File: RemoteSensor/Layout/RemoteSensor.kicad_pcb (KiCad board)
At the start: 2 copper layers, 50.8 x 50.8 mm, 47 parts, among them J1 PRG_HEADER, J2 LCD_HEADER, J3 USB_B_Micro, J4 BATT_CONN, Q1 2N7002, Q2 2N7002, Q3 2N7002, SW1 BTN_RST, SW2 BTN_LOAD, SW3 SW_DPDT_x2, U1 ESP-12F, U2 74LVC2G02, U3 LM50CIM3, U4 MCP73831-2-OT, U5 LM3670MF, U6 BD48ExxG, U7 BD48ExxG

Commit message: Edit layout
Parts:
- removed SW3: SW_DPDT_x2, Switches:SWITCH_DPDT_SMD_AYZ0202
- added C10: 100n, Capacitor_SMD:C_0603_1608Metric_Pad1.05x0.95mm_HandSolder, B.Cu at (130.6, 92.3)
- added C7: 4.7u, Capacitor_SMD:C_0603_1608Metric_Pad1.05x0.95mm_HandSolder, F.Cu at (126.5, 73.1)
- added C8: 47p, Capacitor_SMD:C_0603_1608Metric_Pad1.05x0.95mm_HandSolder, F.Cu at (139.5, 74.0)
- added C9: 47p, Capacitor_SMD:C_0603_1608Metric_Pad1.05x0.95mm_HandSolder, F.Cu at (135.9, 74.0)
- added FB1: Ferrite_Bead, Resistor_SMD:R_0603_1608Metric_Pad1.05x0.95mm_HandSolder, B.Cu at (136.9, 97.0)
- added JP1: Jumper_2_Open, Jumper:SolderJumper-2_P1.3mm_Open_Pad1.0x1.5mm, F.Cu at (148.8, 106.5)
- added JP2: Jumper_2_Open, Jumper:SolderJumper-2_P1.3mm_Open_Pad1.0x1.5mm, F.Cu at (154.5, 106.5)
- added Q4: MMBT2222A-TP, digikey-footprints:SOT-23-3, B.Cu at (129.6, 110.5)
- added Q5: MMBT2222A-TP, digikey-footprints:SOT-23-3, B.Cu at (135.8, 110.5)
- added R17: 1k, Resistor_SMD:R_0603_1608Metric_Pad1.05x0.95mm_HandSolder, F.Cu at (124.3, 85.8)
- added R18: 1k, Resistor_SMD:R_0603_1608Metric_Pad1.05x0.95mm_HandSolder, F.Cu at (126.2, 85.8)
- added R19: 10k, Resistor_SMD:R_0603_1608Metric_Pad1.05x0.95mm_HandSolder, B.Cu at (140.0, 87.1)
- added R20: 10k, Resistor_SMD:R_0603_1608Metric_Pad1.05x0.95mm_HandSolder, F.Cu at (135.2, 87.1)
- added R21: 10k, Resistor_SMD:R_0603_1608Metric_Pad1.05x0.95mm_HandSolder, F.Cu at (143.1, 89.9)
- added R22: 10k, Resistor_SMD:R_0603_1608Metric_Pad1.05x0.95mm_HandSolder, F.Cu at (131.3, 87.1)
- added R23: 10k, Resistor_SMD:R_0603_1608Metric_Pad1.05x0.95mm_HandSolder, B.Cu at (135.8, 107.4)
- added R24: 10k, Resistor_SMD:R_0603_1608Metric_Pad1.05x0.95mm_HandSolder, B.Cu at (129.6, 107.4)
- added R25: 27, Resistor_SMD:R_0603_1608Metric_Pad1.05x0.95mm_HandSolder, F.Cu at (141.3, 74.0)
- added R26: 27, Resistor_SMD:R_0603_1608Metric_Pad1.05x0.95mm_HandSolder, F.Cu at (137.7, 74.0)
- added U10: FT231XS, Package_SO:SSOP-20_3.9x8.7mm_P0.635mm, B.Cu at (131.1, 97.0)
- added U8: LM50CIM3, LM50CIM3:SOT95P260X110-3N, F.Cu at (141.4, 111.1)
- added U9: MCP23008-E_P, Package_SO:SOIC-18W_7.5x11.6mm_P1.27mm, B.Cu at (140.3, 80.2)
- C3: value 4.7u -> 10u
- C4: value 10u -> 4.7u
- J1: value PRG_HEADER -> USB_B_Micro; footprint Connector_PinSocket_2.54mm:PinSocket_1x03_P2.54mm_Vertical -> Connector_USB:USB_Micro-B_Molex_47346-0001
- J2: value LCD_HEADER -> BATT_CONN; footprint Connector_PinHeader_2.54mm:PinHeader_1x04_P2.54mm_Vertical -> Connector_JST:JST_PH_S2B-PH-SM4-TB_1x02-1MP_P2.00mm_Horizontal; moved to B.Cu
- J3: value USB_B_Micro -> LCD_HEADER; footprint Connector_USB:USB_Micro-B_Molex_47346-0001 -> Connector_PinHeader_2.54mm:PinHeader_1x04_P2.54mm_Vertical
- J4: value BATT_CONN -> PRG_HEADER; footprint Connector_JST:JST_PH_S2B-PH-SM4-TB_1x02-1MP_P2.00mm_Horizontal -> Connector_PinSocket_2.54mm:PinSocket_1x03_P2.54mm_Vertical; moved to F.Cu
- L1: footprint Inductor_SMD:L_0603_1608Metric_Pad1.05x0.95mm_HandSolder -> Inductor_SMD:L_Taiyo-Yuden_NR-24xx_HandSoldering
- Q3, R15, R2, R3, R4: moved to F.Cu
- R1: value 10k -> 2k; moved to F.Cu
- R10: value 1k -> 10k
- R11: value 1k -> 4.7k
- R12: value 2k -> 100
- R13: value 10k -> 100; moved to F.Cu
- R14: value 10k -> 4.7k; moved to F.Cu
- R5, R6: value 4.7k -> 10k
- R8, R9: value 220 -> 10k
- SW2: value BTN_LOAD -> SW_Push
- U1: value ESP-12F -> MCP73831-2-OT; footprint RF_Module:ESP-12E -> Package_TO_SOT_SMD:SOT-23-5
- U2: value 74LVC2G02 -> LM3671MF; footprint Package_SO:VSSOP-8_2.3x2mm_P0.5mm -> Package_TO_SOT_SMD:TSOT-23-5; moved to F.Cu
- U3: value LM50CIM3 -> BD48ExxG; footprint LM50CIM3:SOT95P260X110-3N -> Package_TO_SOT_SMD:SOT-23-5
- U4: value MCP73831-2-OT -> BD48ExxG
- U5: value LM3670MF -> LM3671MF
- U6: value BD48ExxG -> 74LVC2G02; footprint Package_TO_SOT_SMD:SOT-23-5 -> Package_SO:VSSOP-8_2.3x2mm_P0.5mm; moved to F.Cu
- U7: value BD48ExxG -> ESP-12F; footprint Package_TO_SOT_SMD:SOT-23-5 -> RF_Module:ESP-12E; moved to F.Cu
- moved R16 48.2 mm to (126.4, 107.8), turned to 180 degrees
- moved R12 45.9 mm to (128.1, 111.7), turned to 0 degrees
- moved J4 43.6 mm to (162.9, 95.0), turned to 0 degrees
- moved R9 34.8 mm to (152.8, 83.5), turned to 270 degrees
- moved U6 32.6 mm to (151.8, 79.1), turned to 0 degrees
- moved R1 31.3 mm to (132.3, 66.8)
- moved U3 30.6 mm to (132.2, 82.2)
- moved Q2 29.7 mm to (151.9, 84.3), turned to 270 degrees
- moved U1 28.5 mm to (128.9, 68.9), turned to 0 degrees
- moved R8 27.1 mm to (151.0, 83.5), turned to 270 degrees
- moved R11 26.9 mm to (142.5, 101.3), turned to 90 degrees
- moved R13 24.4 mm to (151.3, 111.7), turned to 180 degrees
- moved Q1 24.1 mm to (149.8, 67.2), turned to 90 degrees
- moved J3 24.0 mm to (117.8, 77.9), turned to 0 degrees
- moved J1 23.8 mm to (139.7, 68.2), turned to 180 degrees
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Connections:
- C3 pad 1: V_BATT -> 3.3V
- C4 pad 1: 3.3V -> V_USB
- J1 pad 1: Net-(J1-Pad1) -> V_USB
- J1 pad 2: GND -> USBDM
- J1 pad 3: Net-(J1-Pad3) -> USBDP
- J2 pad 1: 3.3V -> V_BATT
- J2 pad 2: Net-(J2-Pad2) -> GND
- J3 pad 1: V_USB -> 3.3V
- J3 pad 2: (no net) -> Net-(J3-Pad2)
- J3 pad 3: (no net) -> /Processor/SCL
- J3 pad 4: (no net) -> /Processor/SDA
- J4 pad 1: GND -> PRG_TX
- J4 pad 2: V_BATT -> GND
- L1 pad 1: Net-(L1-Pad1) -> /Power/SW
- Q1 pad 1: /SLEEP_STS -> V_USB
- Q1 pad 2: /CENTER_PIN -> GND
- Q1 pad 3: /RST -> Net-(Q1-Pad3)
- Q2 pad 1: /WAKE_STS -> SLEEP_STS
- Q2 pad 2: GND -> CENTER_BTN
- Q2 pad 3: Net-(Q2-Pad3) -> RST
- Q3 pad 1: /WAKE_STS -> WAKE_STS
- Q3 pad 3: Net-(J2-Pad2) -> Net-(J3-Pad2)
- R1 pad 1: 3.3V -> Net-(R1-Pad1)
- R1 pad 2: /RST -> GND
- R10 pad 1: Net-(J1-Pad1) -> SLEEP_STS
- R10 pad 2: /PRG_TX -> GND
- R11 pad 1: Net-(J1-Pad3) -> 3.3V
- R11 pad 2: /PRG_RX -> /Processor/SCL
- R12 pad 1: Net-(R12-Pad1) -> HB_PIN
- R12 pad 2: GND -> Net-(D1-Pad2)
- R13 pad 1: /WAKE_STS -> Net-(D2-Pad2)
- R13 pad 2: GND -> BATT_PIN
- R14 pad 2: /CHARGER_STS -> /Processor/SDA
- R15 pad 2: /BATT_STS -> Net-(R15-Pad2)
- R16 pad 2: /CHARGE_STS -> RST
- R2 pad 1: /SLEEP_PIN -> 3.3V
- R2 pad 2: GND -> CHARGE_STS
- R3 pad 1: /HB_PIN -> 3.3V
- R3 pad 2: GND -> BATT_STS
- R4 pad 1: /SLEEP_STS -> 3.3V
- R4 pad 2: GND -> CHARGER_STS
- R5 pad 1: 3.3V -> V_USB
- R5 pad 2: /SCL -> GND
- R6 pad 1: 3.3V -> V_BATT
- R6 pad 2: /SDA -> Net-(Q1-Pad3)
- R7 pad 1: 3.3V -> SLEEP_PIN
- R7 pad 2: Net-(R7-Pad2) -> GND
- R8 pad 1: /HB_PIN -> WAKE_STS
- R8 pad 2: Net-(D1-Pad2) -> GND
- R9 pad 1: Net-(D2-Pad2) -> HB_PIN
- R9 pad 2: /BATT_PIN -> GND
- S1 pad 1: /UP_PIN -> UP_BTN
- S1 pad 2: /DOWN_PIN -> DOWN_BTN
- S1 pad T: /CENTER_PIN -> CENTER_BTN
- SW1 pad 1: /RST -> RST
- SW2 pad 1: Net-(SW2-Pad1) -> FLASH
- U1 pad 1: /RST -> CHARGE_STS
- U1 pad 2: /TEMP_PIN -> GND
- U1 pad 3: Net-(R7-Pad2) -> V_BATT
- U1 pad 4: /RST -> V_USB
- U1 pad 5: /BATT_STS -> Net-(R1-Pad1)
- U2 pad 1: /SLEEP_PIN -> V_USB
- U2 pad 2: /SLEEP_STS -> GND
- U2 pad 3: /SLEEP_STS -> V_USB
- U2 pad 4: GND -> 3.3V
- U2 pad 5: /WAKE_STS -> /Power/SW
- U3 pad 1: 3.3V -> BATT_STS
- U3 pad 2: /TEMP_PIN -> V_BATT
- U3 pad 3: Net-(Q2-Pad3) -> GND
- U4 pad 1: /CHARGE_STS -> CHARGER_STS
- U4 pad 2: GND -> V_USB
- U4 pad 3: V_BATT -> GND
- U4 pad 4: V_USB -> (no net)
- U4 pad 5: Net-(R12-Pad1) -> (no net)
- U5 pad 3: V_BATT -> Net-(Q1-Pad3)
- U5 pad 5: Net-(L1-Pad1) -> /Power/SW
- U6 pad 1: /CHARGER_STS -> SLEEP_PIN
- U6 pad 2: 3.3V -> SLEEP_STS
- U6 pad 3: GND -> SLEEP_STS
- U6 pad 4: (no net) -> GND
- U6 pad 5: (no net) -> WAKE_STS
- U7 pad 1: /BATT_STS -> RST
- U7 pad 2: 3.3V -> /Processor/TEMP_PIN
- U7 pad 3: GND -> Net-(R15-Pad2)
- U7 pad 4: (no net) -> RST

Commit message: New PCB layout
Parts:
- C8, C9, JP1, JP2, Q3, R10, R11, R14, R17, R18, R21, R25, R26, R3, R4, R7, R8, R9, U3, U4, U6: moved to B.Cu
- R19, U9: moved to F.Cu
- moved J3 47.8 mm to (162.7, 94.2)
- moved Q3 40.4 mm to (156.8, 97.8), turned to 90 degrees
- moved J4 32.3 mm to (132.8, 83.1), turned to 270 degrees
- moved JP2 27.5 mm to (145.4, 80.5), turned to 270 degrees
- moved JP1 26.9 mm to (141.5, 80.5), turned to 270 degrees
- moved FB1 26.6 mm to (130.7, 71.1), turned to 0 degrees
- moved R23 23.9 mm to (144.8, 85.3)
- moved R24 23.9 mm to (138.6, 85.3)
- moved Q4 23.9 mm to (138.6, 88.4)
- moved Q5 23.9 mm to (144.8, 88.4)
- moved C10 22.1 mm to (125.7, 70.7), turned to 90 degrees
- moved U9 20.6 mm to (150.6, 98.0), turned to 0 degrees
- moved U10 20.3 mm to (130.7, 76.7), turned to 0 degrees
- moved U6 18.7 mm to (147.8, 97.4), turned to 180 degrees
- moved SW2 17.4 mm to (152.0, 81.9), turned to 90 degrees
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
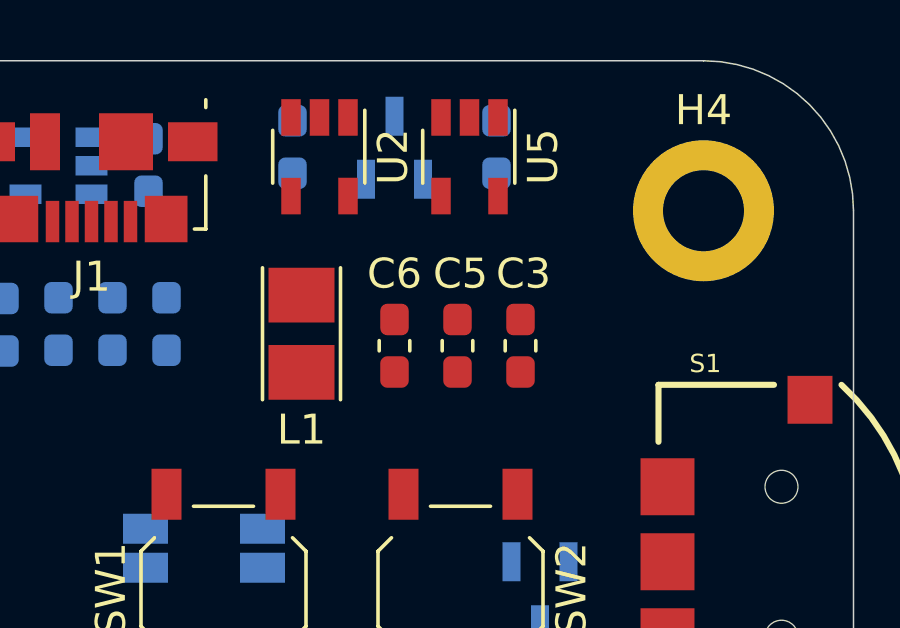
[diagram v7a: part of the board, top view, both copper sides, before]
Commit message: Change the USB switching regulator for an LDO
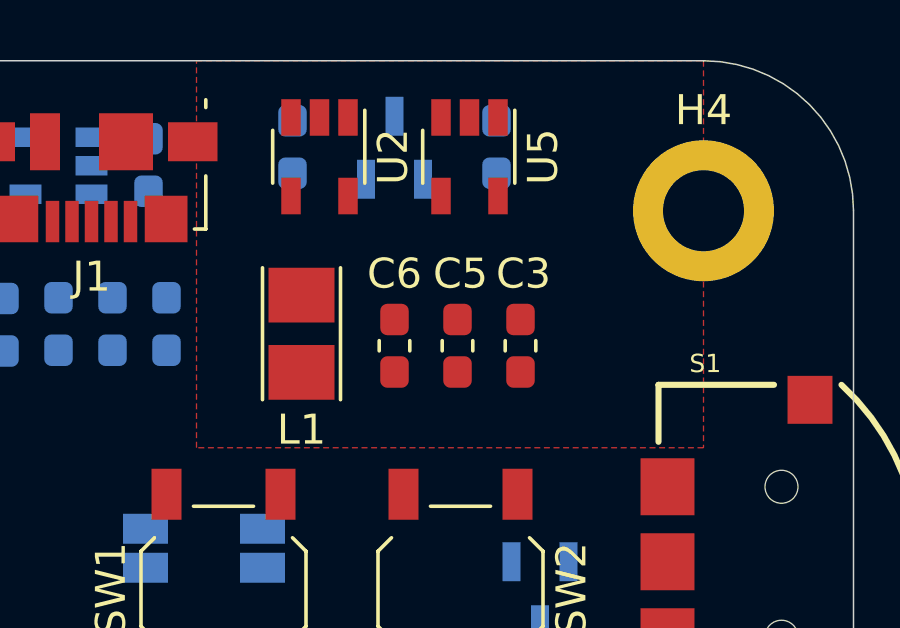
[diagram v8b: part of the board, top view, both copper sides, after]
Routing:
- added copper zone on F.Cu, net GND
